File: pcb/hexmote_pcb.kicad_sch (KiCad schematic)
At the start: 17 parts, among them J2 LiPo Cell, J3 Conn_01x10_Pin, SW1 SW_Push, SW10 SW_SPDT, SW2 SW_Push, SW3 SW_Push, SW4 SW_Push, SW5 SW_Push, SW6 SW_Push, SW7 SW_Push, SW8 SW_Push, U1 SuperMini nRF52840, U2 Joystick

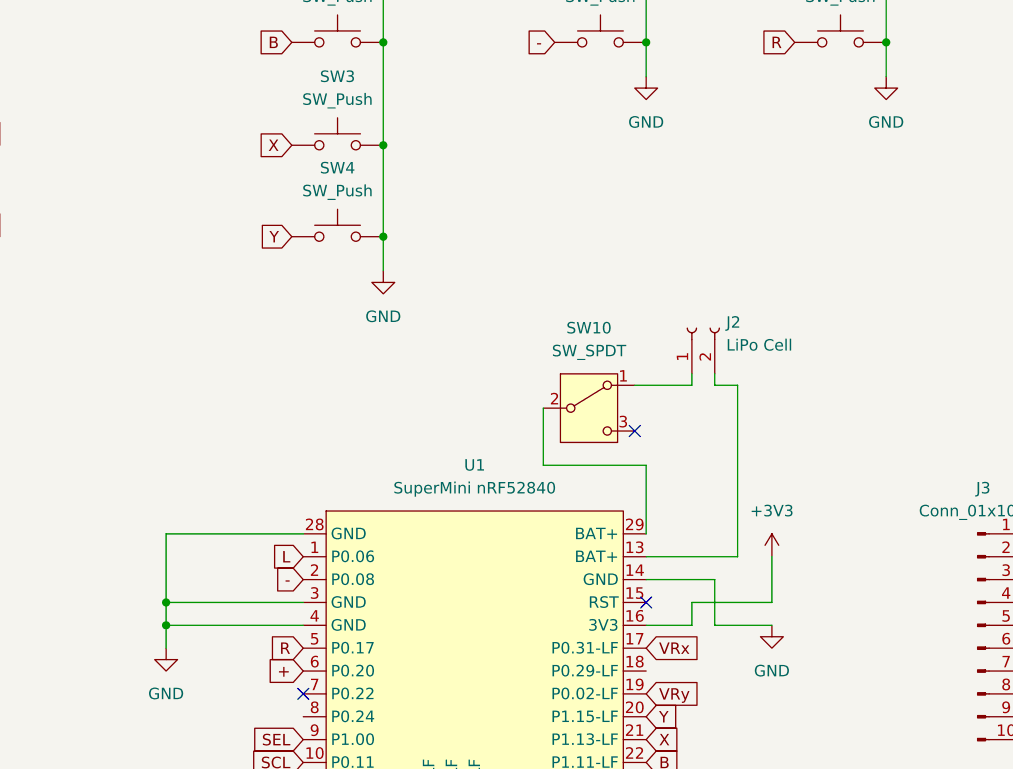
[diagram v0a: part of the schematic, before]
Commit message: added solder jumper to allow for configuration of battery
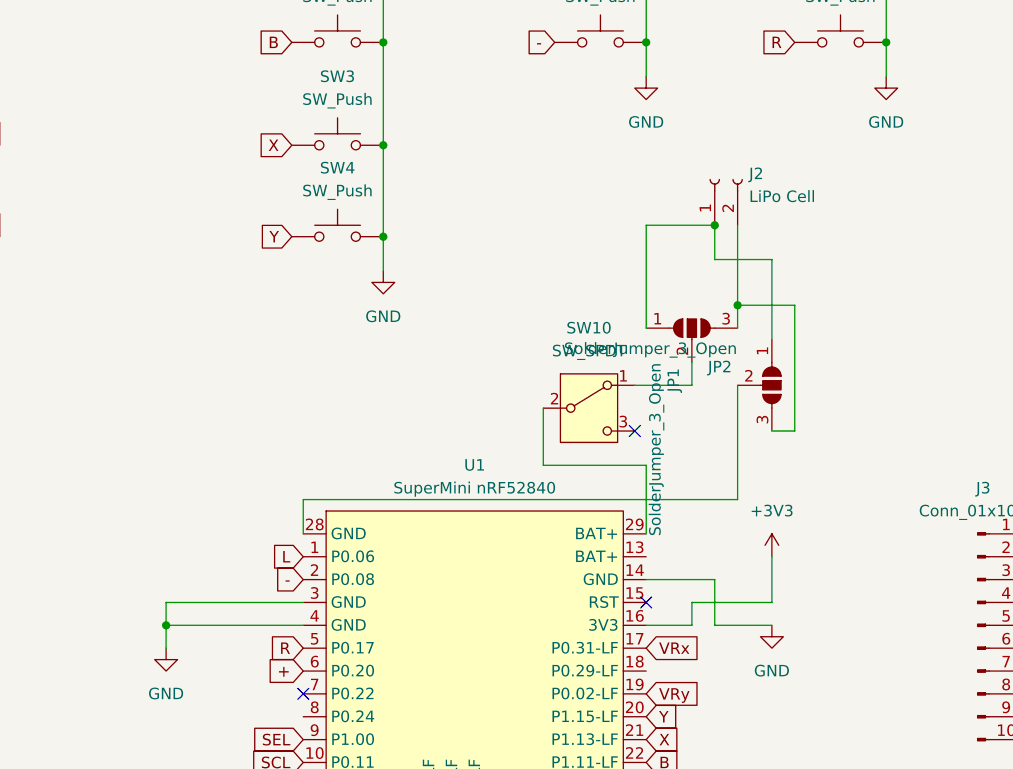
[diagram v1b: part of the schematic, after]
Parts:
- added JP1, JP2: SolderJumper_3_Open, Jumper:SolderJumper-3_P1.3mm_Open_Pad1.0x1.5mm_NumberLabels, symbol Jumper:SolderJumper_3_Open
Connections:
- net GND: no longer U1.28 (GND)
- net at U1.13 (BAT+): no longer J2.2 (Pin_2)
- net at J2.1 (Pin_1): now also JP1.1 (A), JP2.1 (A); no longer SW10.1 (A)
- new net: JP2.2 (C), U1.28 (GND)
- new net: J2.2 (Pin_2), JP1.3 (B), JP2.3 (B)
- new net: JP1.2 (C), SW10.1 (A)
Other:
- moved on the sheet: J2
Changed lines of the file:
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@@
 	(paper "A4")
+	(junction
+		(at 162.56 95.25)
+		(diameter 0)
+		(color 0 0 0 0)
+	)
 	(junction
 		(at 125.73 86.36)
@@
 	)
 	(junction
+		(at 165.1 104.14)
+		(diameter 0)
+		(color 0 0 0 0)
+	)
+	(junction
 		(at 207.01 142.24)
 		(diameter 0)
@@
 	)
 	(junction
-		(at 101.6 137.16)
-		(diameter 0)
-		(color 0 0 0 0)
-	)
-	(junction
 		(at 73.66 100.33)
 		(diameter 0)
@@
 	(wire
 		(pts
-			(xy 101.6 129.54) (xy 101.6 137.16)
+			(xy 162.56 99.06) (xy 168.91 99.06)
 		)
 		(stroke
@@
 	(wire
 		(pts
+			(xy 165.1 104.14) (xy 165.1 106.68)
+		)
+		(stroke
+			(width 0)
+			(type default)
+		)
+	)
+	(wire
+		(pts
+			(xy 165.1 95.25) (xy 165.1 104.14)
+		)
+		(stroke
+			(width 0)
+			(type default)
+		)
+	)
+	(wire
+		(pts
 			(xy 71.12 100.33) (xy 73.66 100.33)
 		)
@@
 	(wire
 		(pts
-			(xy 162.56 113.03) (xy 162.56 111.76)
-		)
-		(stroke
-			(width 0)
-			(type default)
-		)
-	)
-	(wire
-		(pts
 			(xy 196.85 139.7) (xy 204.47 139.7)
 		)
@@
 	(wire
 		(pts
-			(xy 165.1 113.03) (xy 162.56 113.03)
-		)
-		(stroke
-			(width 0)
-			(type default)
-		)
-	)
-	(wire
-		(pts
 			(xy 74.93 107.95) (xy 74.93 113.03)
 		)
@@
 	(wire
 		(pts
+			(xy 171.45 118.11) (xy 168.91 118.11)
+		)
+		(stroke
+			(width 0)
+			(type default)
+		)
+	)
+	(wire
+		(pts
 			(xy 71.12 90.17) (xy 73.66 90.17)
 		)
@@
 	(wire
 		(pts
-			(xy 165.1 132.08) (xy 154.94 132.08)
+			(xy 165.1 104.14) (xy 171.45 104.14)
 		)
 		(stroke
@@
 	(wire
 		(pts
-			(xy 116.84 129.54) (xy 101.6 129.54)
-		)
-		(stroke
-			(width 0)
-			(type default)
-		)
-	)
-	(wire
-		(pts
 			(xy 125.73 96.52) (xy 125.73 100.33)
 		)
@@
 	(wire
 		(pts
+			(xy 162.56 95.25) (xy 162.56 99.06)
+		)
+		(stroke
+			(width 0)
+			(type default)
+		)
+	)
+	(wire
+		(pts
+			(xy 154.94 95.25) (xy 154.94 106.68)
+		)
+		(stroke
+			(width 0)
+			(type default)
+		)
+	)
+	(wire
+		(pts
 			(xy 153.67 113.03) (xy 160.02 113.03)
 		)
@@
 	(wire
 		(pts
+			(xy 162.56 95.25) (xy 154.94 95.25)
+		)
+		(stroke
+			(width 0)
+			(type default)
+		)
+	)
+	(wire
+		(pts
 			(xy 154.94 121.92) (xy 154.94 129.54)
 		)
@@
 	(wire
 		(pts
+			(xy 116.84 125.73) (xy 165.1 125.73)
+		)
+		(stroke
+			(width 0)
+			(type default)
+		)
+	)
+	(wire
+		(pts
 			(xy 204.47 129.54) (xy 201.93 129.54)
 		)
@@
 	(wire
 		(pts
-			(xy 160.02 113.03) (xy 160.02 111.76)
-		)
-		(stroke
-			(width 0)
-			(type default)
-		)
-	)
-	(wire
-		(pts
 			(xy 207.01 143.51) (xy 207.01 142.24)
 		)
@@
 	(wire
 		(pts
+			(xy 116.84 125.73) (xy 116.84 129.54)
+		)
+		(stroke
+			(width 0)
+			(type default)
+		)
+	)
+	(wire
+		(pts
 			(xy 160.02 139.7) (xy 160.02 137.16)
 		)
@@
 	(wire
 		(pts
+			(xy 171.45 104.14) (xy 171.45 118.11)
+		)
+		(stroke
+			(width 0)
+			(type default)
+		)
+	)
+	(wire
+		(pts
+			(xy 168.91 99.06) (xy 168.91 107.95)
+		)
+		(stroke
+			(width 0)
+			(type default)
+		)
+	)
+	(wire
+		(pts
 			(xy 212.09 137.16) (xy 196.85 137.16)
 		)
@@
 	(wire
 		(pts
+			(xy 165.1 113.03) (xy 165.1 125.73)
+		)
+		(stroke
+			(width 0)
+			(type default)
+		)
+	)
+	(wire
+		(pts
 			(xy 204.47 139.7) (xy 204.47 129.54)
 		)
@@
 	(wire
 		(pts
-			(xy 165.1 113.03) (xy 165.1 132.08)
+			(xy 160.02 110.49) (xy 160.02 113.03)
 		)
 		(stroke
@@
 	(symbol
 		(lib_id "Connector:Conn_01x02_Socket")
-		(at 160.02 106.68 90)
+		(at 162.56 90.17 90)
 		(unit 1)
 		(exclude_from_sim no)
@@
 		(fields_autoplaced yes)
 		(property "Reference" "J2"
-			(at 163.83 106.0449 90)
+			(at 166.37 89.5349 90)
 			(effects
 				(font
@@
 		)
 		(property "Value" "LiPo Cell"
-			(at 163.83 108.5849 90)
+			(at 166.37 92.0749 90)
 			(effects
 				(font
@@
 		)
 		(property "Footprint" "Connector_JST:JST_PH_S2B-PH-K_1x02_P2.00mm_Horizontal"
-			(at 160.02 106.68 0)
+			(at 162.56 90.17 0)
 			(effects
 				(font
@@
 		)
 		(property "Datasheet" "~"
-			(at 160.02 106.68 0)
+			(at 162.56 90.17 0)
 			(effects
 				(font
@@
 		)
 		(property "Description" "Generic connector, single row, 01x02, script generated"
-			(at 160.02 106.68 0)
+			(at 162.56 90.17 0)
 			(effects
 				(font
@@
 					(unit 1)
 				)
+			)
+		)
+	)
+	(symbol
+		(lib_id "Jumper:SolderJumper_3_Open")
+		(at 168.91 113.03 270)
+		(unit 1)
+		(exclude_from_sim no)
+		(in_bom no)
+		(on_board yes)
+		(dnp no)
+		(property "Reference" "JP2"
+			(at 161.798 110.998 90)
+			(effects
+				(font
+					(size 1.27 1.27)
+				)
+				(justify left)
+			)
+		)
+		(property "Value" "SolderJumper_3_Open"
+			(at 145.796 108.966 90)
+			(effects
+				(font
+					(size 1.27 1.27)
+				)
+				(justify left)
+			)
+		)
+		(property "Footprint" "Jumper:SolderJumper-3_P1.3mm_Open_Pad1.0x1.5mm_NumberLabels"
+			(at 168.91 113.03 0)
+			(effects
+				(font
+					(size 1.27 1.27)
+				)
+				(hide yes)
+			)
+		)
+		(property "Datasheet" "~"
+			(at 168.91 113.03 0)
+			(effects
+				(font
+					(size 1.27 1.27)
+				)
+				(hide yes)
+			)
+		)
+		(property "Description" "Solder Jumper, 3-pole, open"
+			(at 168.91 113.03 0)
+			(effects
+				(font
+					(size 1.27 1.27)
+				)
+				(hide yes)
+			)
+		)
+		(pin "1"
+		)
+		(pin "2"
+		)
+		(pin "3"
+		)
+		(instances
+			(project "hexmote_pcb"
+				(path "/cd907341-f341-412c-9f24-14ef05b21a1f"
+					(reference "JP2")
+					(unit 1)
+				)
+			)
+		)
+	)
+	(symbol
+		(lib_id "Jumper:SolderJumper_3_Open")
+		(at 160.02 106.68 0)
+		(unit 1)
+		(exclude_from_sim no)
+		(in_bom no)
+		(on_board yes)
+		(dnp no)
+		(property "Reference" "JP1"
+			(at 157.988 113.792 90)
+			(effects
+				(font
+					(size 1.27 1.27)
+				)
+				(justify left)
+			)
+		)
+		(property "Value" "SolderJumper_3_Open"
+			(at 155.956 129.794 90)
+			(effects
+				(font
+					(size 1.27 1.27)
+				)
+				(justify left)
+			)
+		)
+		(property "Footprint" "Jumper:SolderJumper-3_P1.3mm_Open_Pad1.0x1.5mm_NumberLabels"
+			(at 160.02 106.68 0)
+			(effects
+				(font
+					(size 1.27 1.27)
+				)
+				(hide yes)
+			)
+		)
+		(property "Datasheet" "~"
+			(at 160.02 106.68 0)
+			(effects
+				(font
+					(size 1.27 1.27)
+				)
+				(hide yes)
+			)
+		)
+		(property "Description" "Solder Jumper, 3-pole, open"
+			(at 160.02 106.68 0)
+			(effects
+				(font
+					(size 1.27 1.27)
+				)
+				(hide yes)
+			)
+		)
+		(pin "1"
+		)
+		(pin "2"
+		)
+		(pin "3"
+		)
+		(instances
+			(project ""
+				(path "/cd907341-f341-412c-9f24-14ef05b21a1f"
+					(reference "JP1")
+					(unit 1)
+				)

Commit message: changed somethings for case
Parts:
- SW7, SW8: footprint Button_Switch_THT:SW_Tactile_SPST_Angled_PTS645Vx58-2LFS -> Button_Switch_THT:SW_Tactile_SPST_Angled_PTS645Vx83-2LFS
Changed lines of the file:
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@@
 			)
 		)
-		(property "Footprint" "Button_Switch_THT:SW_Tactile_SPST_Angled_PTS645Vx58-2LFS"
+		(property "Footprint" "Button_Switch_THT:SW_Tactile_SPST_Angled_PTS645Vx83-2LFS"
 			(at 176.53 59.69 0)
 			(effects
@@
 			)
 		)
-		(property "Footprint" "Button_Switch_THT:SW_Tactile_SPST_Angled_PTS645Vx58-2LFS"
+		(property "Footprint" "Button_Switch_THT:SW_Tactile_SPST_Angled_PTS645Vx83-2LFS"
 			(at 176.53 69.85 0)
 			(effects
